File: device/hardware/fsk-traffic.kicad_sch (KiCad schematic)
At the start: 35 parts, among them J1 JTAG, J2 USB_C, J3 5268-03AX, J4 5268-03AX, J5 5268-03AX, Q1 MMBT5551, Q2 MMBT5401, Q3 MMBT5551, Q4 MMBT5401, U1 XC6206P332MR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

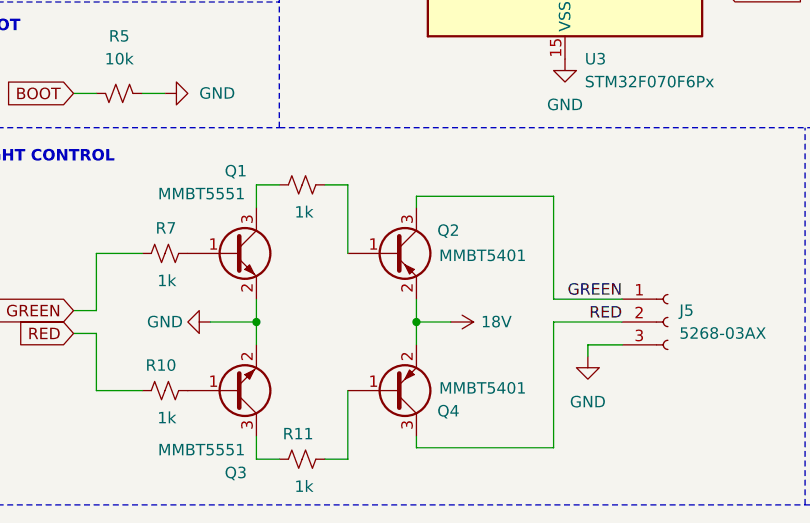
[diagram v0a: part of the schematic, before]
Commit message: fix: missing pullup on PNP base cause overcurrent
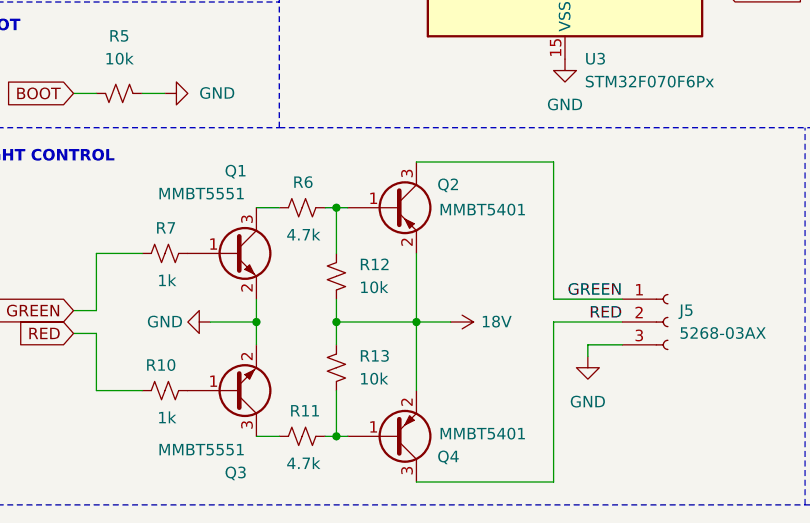
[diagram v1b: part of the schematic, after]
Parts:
- added R12, R13: 10k, Resistor_SMD:R_0603_1608Metric, symbol Device:R_Small_US
- R11, R6: value 1k -> 4.7k
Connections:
- net 18V: now also R12.2, R13.1
- net at Q2.1 (B), R6.1: now also R12.1
- net at Q4.1 (B), R11.1: now also R13.2
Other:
- moved on the sheet: Q2, Q4, R11

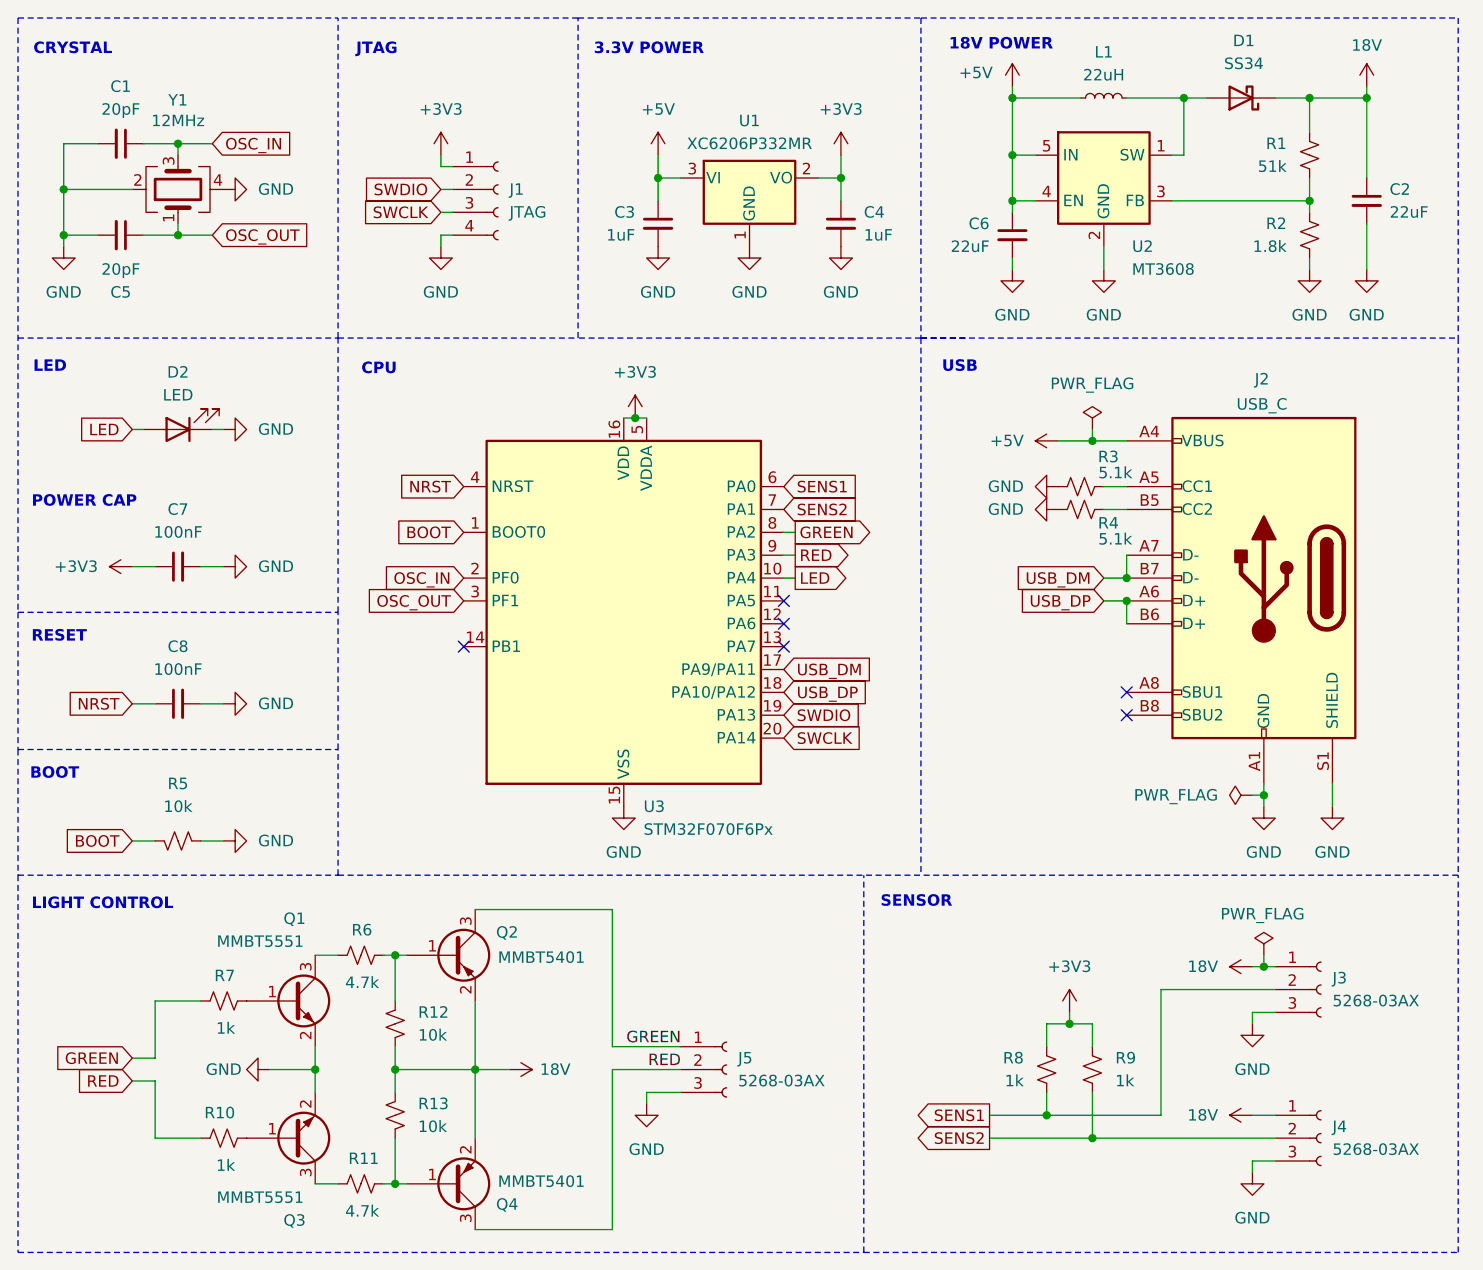
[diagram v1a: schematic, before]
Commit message: update: PCB v2
fix SSR Hi-side driver and MT3608 layout
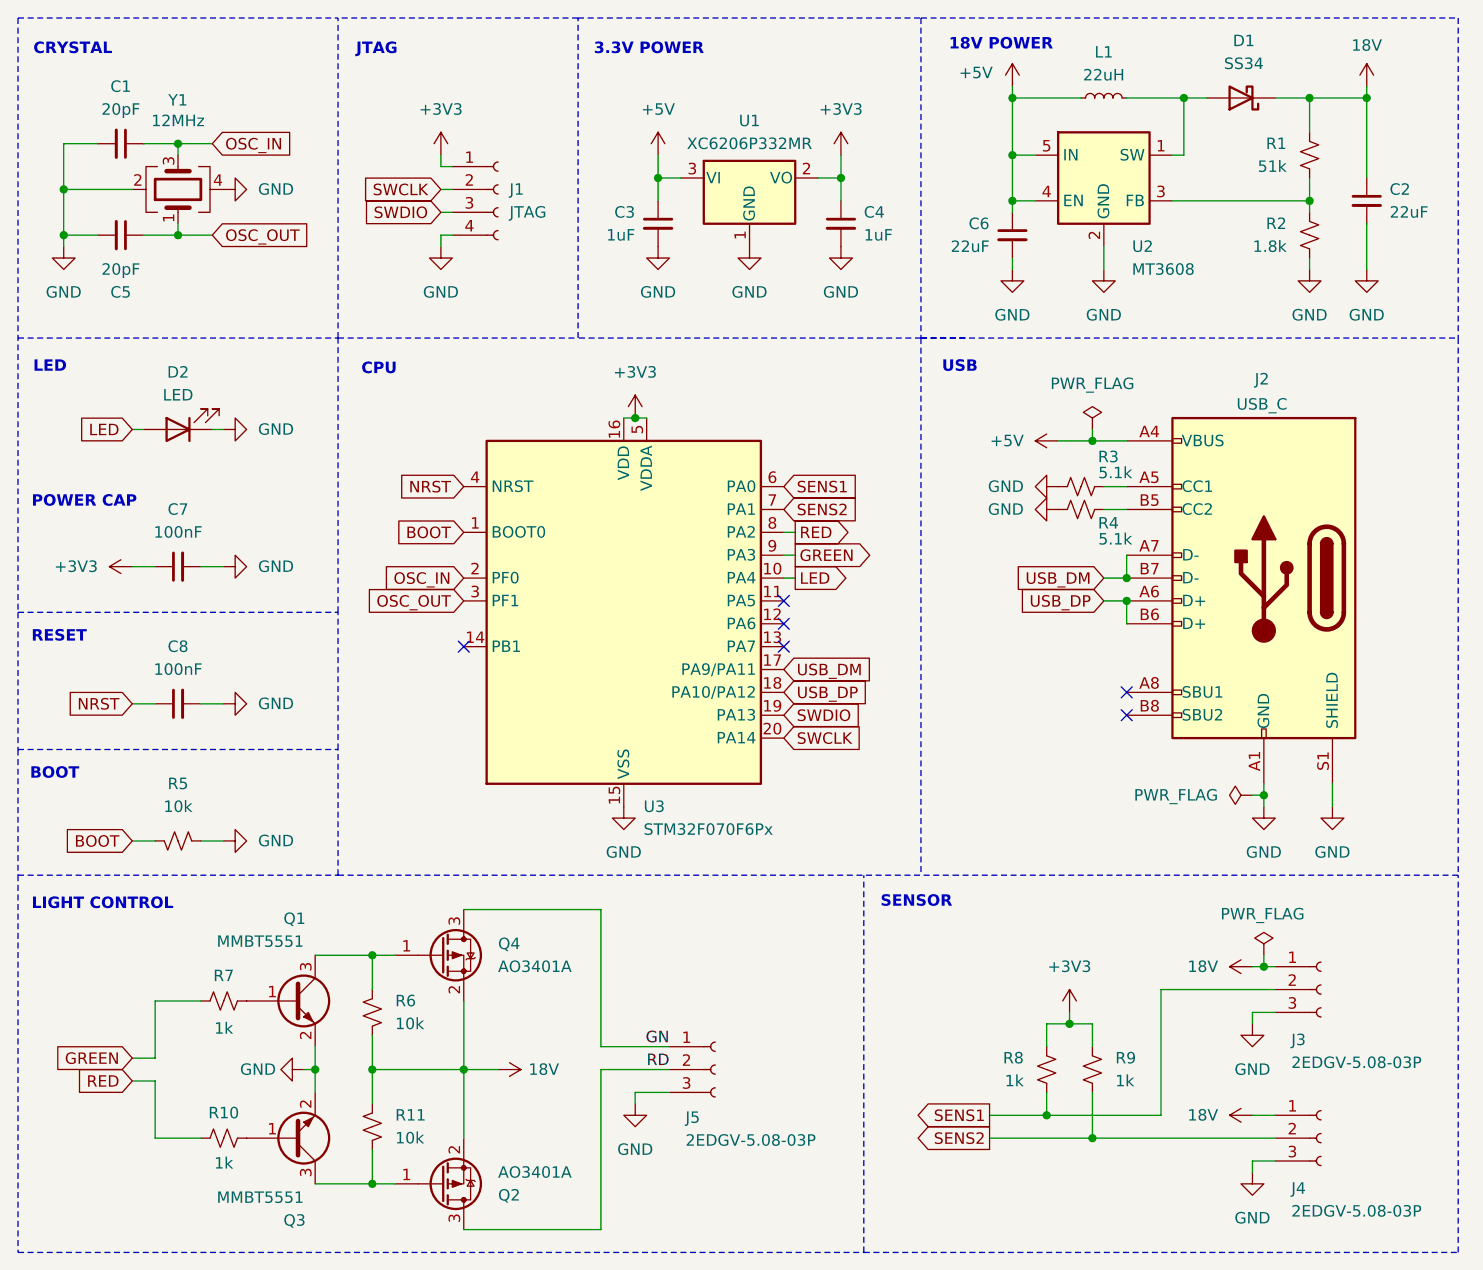
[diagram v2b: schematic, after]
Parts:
- removed Q2, Q4: MMBT5401, Package_TO_SOT_SMD:SOT-23, symbol Device:Q_PNP_BEC
- removed R12, R13: 10k, Resistor_SMD:R_0603_1608Metric, symbol Device:R_Small_US
- added Q2, Q4: AO3401A, Package_TO_SOT_SMD:SOT-23, symbol Transistor_FET:AO3401A
- J3, J4, J5: value 5268-03AX -> 2EDGV-5.08-03P; footprint Connector_Molex:Molex_SPOX_5268-03A_1x03_P2.50mm_Horizontal -> TerminalBlock_Phoenix:TerminalBlock_Phoenix_MKDS-1,5-3-5.08_1x03_P5.08mm_Horizontal
- R11, R6: value 4.7k -> 10k; LCSC C21190 -> C25804
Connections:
- net 18V: now also R11.1, R6.2, Q2.2 (S), Q4.2 (S)
- net GREEN: now also U3.9 (PA3); no longer J5.1 (Pin_1), U3.8 (PA2)
- net RED: now also U3.8 (PA2); no longer J5.2 (Pin_2), U3.9 (PA3)
- net SWCLK: now also J1.2 (Pin_2); no longer J1.3 (Pin_3)
- net SWDIO: now also J1.3 (Pin_3); no longer J1.2 (Pin_2)
- net at R6.1: now also Q1.3 (C), Q4.1 (G)
- net at Q3.3 (C), R11.2: now also Q2.1 (G)
- new net GN: J5.1 (Pin_1), Q4.3 (D)
- new net RD: J5.2 (Pin_2), Q2.3 (D)
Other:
- moved on the sheet: J5

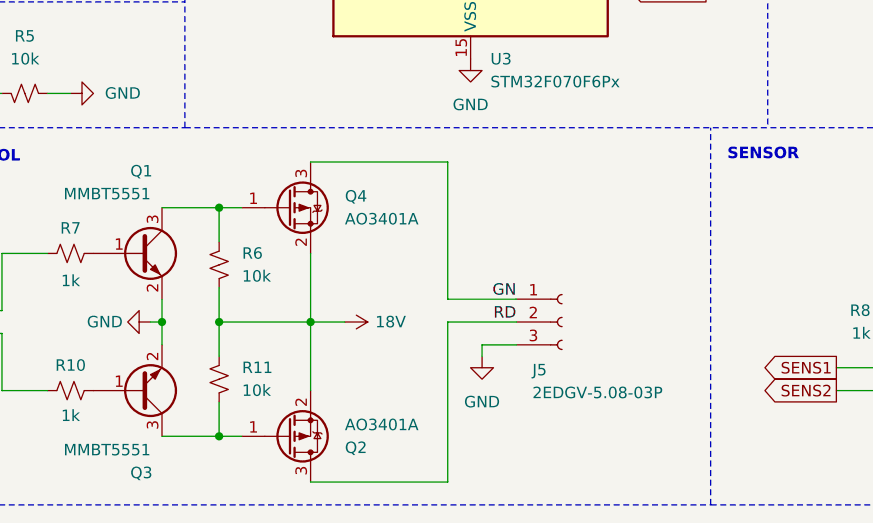
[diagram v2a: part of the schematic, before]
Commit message: fix: add resistor divider to protect PMOS
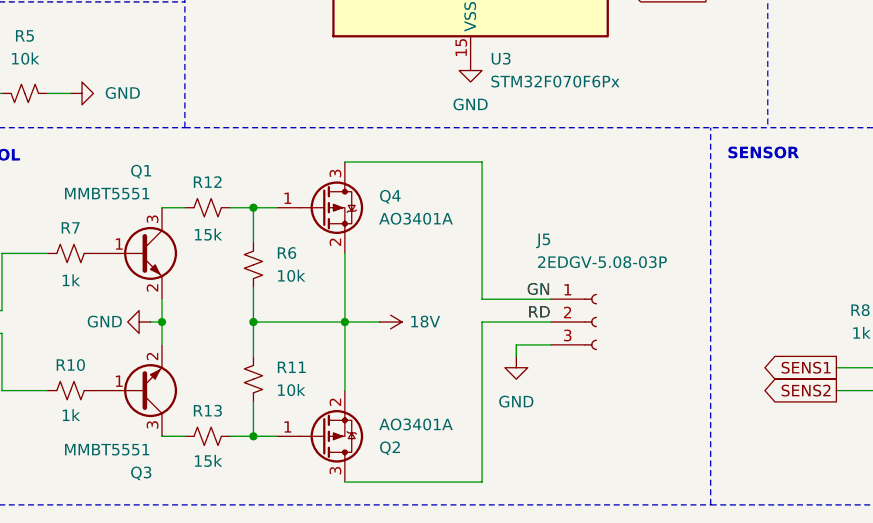
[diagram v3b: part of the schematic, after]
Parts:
- added R12, R13: 15k, Resistor_SMD:R_0603_1608Metric, symbol Device:R_Small_US
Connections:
- net at Q2.1 (G), R11.2: now also R13.1; no longer Q3.3 (C)
- net at Q4.1 (G), R6.1: now also R12.1; no longer Q1.3 (C)
- new net: Q3.3 (C), R13.2
- new net: Q1.3 (C), R12.2
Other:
- moved on the sheet: J5, Q2, Q4, R11, R6

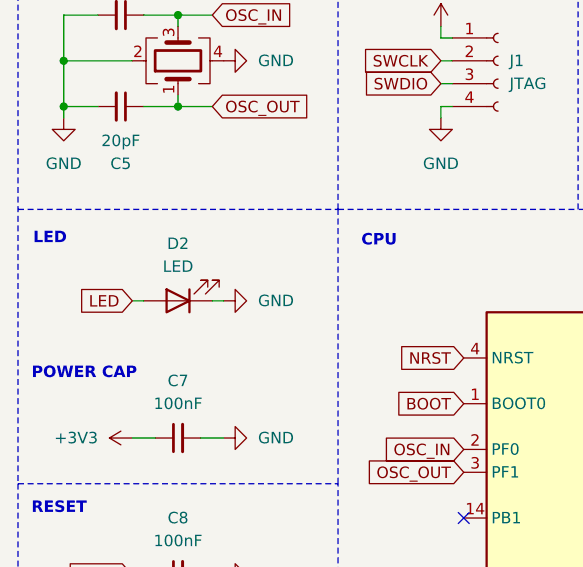
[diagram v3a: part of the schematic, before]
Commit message: fix: misc pcb bugs
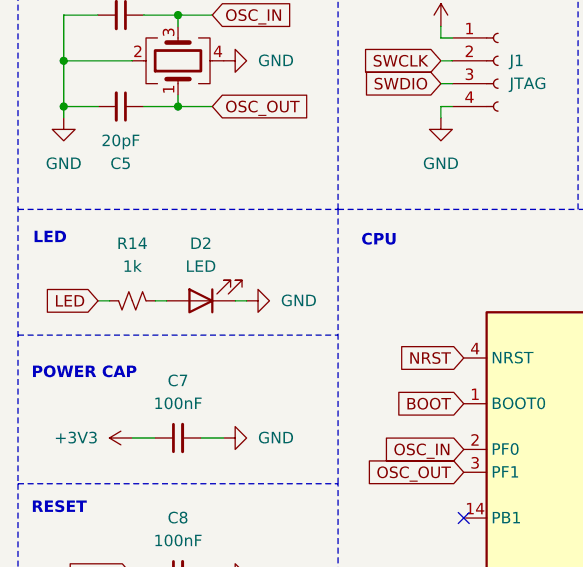
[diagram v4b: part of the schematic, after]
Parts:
- added R14: 1k, Resistor_SMD:R_0603_1608Metric, symbol Device:R_Small_US
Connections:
- net LED: now also R14.2; no longer D2.2 (A)
- new net: D2.2 (A), R14.1
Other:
- moved on the sheet: D2
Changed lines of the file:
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@@
 	(wire
 		(pts
-			(xy 88.9 67.31) (xy 90.17 67.31)
+			(xy 91.44 67.31) (xy 92.71 67.31)
 		)
 		(stroke
@@
 	(wire
 		(pts
-			(xy 80.01 67.31) (xy 81.28 67.31)
+			(xy 76.2 67.31) (xy 77.47 67.31)
 		)
 		(stroke
@@
 		)
 	)
+	(polyline
+		(pts
+			(xy 67.31 71.12) (xy 102.87 71.12)
+		)
+		(stroke
+			(width 0)
+			(type dash)
+		)
+	)
 	(wire
 		(pts
@@
 		)
 	)
+	(wire
+		(pts
+			(xy 82.55 67.31) (xy 83.82 67.31)
+		)
+		(stroke
+			(width 0)
+			(type default)
+		)
+	)
 	(polyline
 		(pts
@@
 	(global_label "LED"
 		(shape input)
-		(at 80.01 67.31 180)
+		(at 76.2 67.31 180)
 		(fields_autoplaced yes)
 		(effects
@@
 		)
 		(property "Intersheetrefs" "${INTERSHEET_REFS}"
-			(at 73.5777 67.31 0)
+			(at 69.7677 67.31 0)
 			(effects
 				(font
@@
 	(symbol
 		(lib_id "power:GND")
-		(at 90.17 67.31 90)
+		(at 92.71 67.31 90)
 		(mirror x)
 		(unit 1)
@@
 		(fields_autoplaced yes)
 		(property "Reference" "#PWR016"
-			(at 96.52 67.31 0)
+			(at 99.06 67.31 0)
 			(effects
 				(font
@@
 		)
 		(property "Value" "GND"
-			(at 93.98 67.3099 90)
+			(at 96.52 67.3099 90)
 			(effects
 				(font
@@
 		)
 		(property "Footprint" ""
-			(at 90.17 67.31 0)
+			(at 92.71 67.31 0)
 			(effects
 				(font
@@
 		)
 		(property "Datasheet" ""
-			(at 90.17 67.31 0)
+			(at 92.71 67.31 0)
 			(effects
 				(font
@@
 		)
 		(property "Description" "Power symbol creates a global label with name \"GND\" , ground"
-			(at 90.17 67.31 0)
+			(at 92.71 67.31 0)
 			(effects
 				(font
@@
 	(symbol
 		(lib_id "Device:LED")
-		(at 85.09 67.31 180)
+		(at 87.63 67.31 180)
 		(unit 1)
 		(exclude_from_sim no)
@@
 		(dnp no)
 		(property "Reference" "D2"
-			(at 85.09 60.96 0)
+			(at 87.63 60.96 0)
 			(effects
 				(font
@@
 		)
 		(property "Value" "LED"
-			(at 85.09 63.5 0)
+			(at 87.63 63.5 0)
 			(effects
 				(font
@@
 		)
 		(property "Footprint" "LED_SMD:LED_0603_1608Metric"
-			(at 85.09 67.31 0)
+			(at 87.63 67.31 0)
 			(effects
 				(font
@@
 		)
 		(property "Datasheet" "~"
-			(at 85.09 67.31 0)
+			(at 87.63 67.31 0)
 			(effects
 				(font
@@
 		)
 		(property "Description" "Light emitting diode"
-			(at 85.09 67.31 0)
+			(at 87.63 67.31 0)
 			(effects
 				(font
@@
 		)
 		(property "LCSC" "C2286"
-			(at 85.09 60.96 0)
+			(at 87.63 60.96 0)
 			(effects
 				(font
@@
 					(unit 1)
 				)
+			)
+		)
+	)
+	(symbol
+		(lib_id "Device:R_Small_US")
+		(at 80.01 67.31 270)
+		(mirror x)
+		(unit 1)
+		(exclude_from_sim no)
+		(in_bom yes)
+		(on_board yes)
+		(dnp no)
+		(property "Reference" "R14"
+			(at 80.01 60.96 90)
+			(effects
+				(font
+					(size 1.27 1.27)
+				)
+			)
+		)
+		(property "Value" "1k"
+			(at 80.01 63.5 90)
+			(effects
+				(font
+					(size 1.27 1.27)
+				)
+			)
+		)
+		(property "Footprint" "Resistor_SMD:R_0603_1608Metric"
+			(at 80.01 67.31 0)
+			(effects
+				(font
+					(size 1.27 1.27)
+				)
+				(hide yes)
+			)
+		)
+		(property "Datasheet" "~"
+			(at 80.01 67.31 0)
+			(effects
+				(font
+					(size 1.27 1.27)
+				)
+				(hide yes)
+			)
+		)
+		(property "Description" "Resistor, small US symbol"
+			(at 80.01 67.31 0)
+			(effects
+				(font
+					(size 1.27 1.27)
+				)
+				(hide yes)
+			)
+		)
+		(property "LCSC" "C21190"
+			(at 80.01 60.96 0)
+			(effects
+				(font
+					(size 1.27 1.27)
+				)
+				(hide yes)
+			)
+		)
+		(pin "2"
+		)
+		(pin "1"
+		)
+		(instances
+			(project "fsk-traffic"
+				(path "/526aa4f3-2c60-4c86-8f21-d15d9dc963dc"
+					(reference "R14")
+					(unit 1)
+				)

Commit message: fix: isolation & filter
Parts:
- removed J3, J4, J5: 2EDGV-5.08-03P, TerminalBlock_Phoenix:TerminalBlock_Phoenix_MKDS-1,5-3-5.08_1x03_P5.08mm_Horizontal, symbol Connector:Conn_01x03_Socket
- added C10, C9: 470nF, Capacitor_SMD:C_0603_1608Metric, symbol Device:C_Small
- added J3, J4, J5: Molex 5569-04A1, Connector_Molex:Molex_Mini-Fit_Jr_5569-04A1_2x02_P4.20mm_Horizontal, symbol Connector:Conn_01x04_Socket
- added R15, R16: 2k, Resistor_SMD:R_0603_1608Metric, symbol Device:R_Small_US
- added U4, U5: LTV-817S, Package_DIP:SMDIP-4_W9.53mm, symbol Isolator:LTV-817S
- R8, R9: value 1k -> 3.3k; LCSC C21190 -> C22978
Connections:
- net +3V3: now also R8.2; no longer R8.1
- net 18V: now also J3.1 (Pin_1), J4.1 (Pin_1), J4.2 (Pin_2), R15.1, R16.1
- net GN: now also J5.4 (Pin_4)
- net GND: now also C10.2, C9.1, J3.4 (Pin_4), J4.4 (Pin_4), J5.1 (Pin_1), U4.3, U5.3
- net RD: now also J5.3 (Pin_3)
- net SENS1: now also R8.1, C10.1, U4.4; no longer R8.2
- net SENS2: now also C9.2, U5.4
- new net: J4.3 (Pin_3), U5.2
- new net: R15.2, U4.1
- new net: R16.2, U5.1
- new net: J3.3 (Pin_3), U4.2
- no-connect marks 6 -> 8
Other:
- moved on the sheet: C1, C2, C3, C4, C5, C6, D1, J1, J2, L1, Q1, Q2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
